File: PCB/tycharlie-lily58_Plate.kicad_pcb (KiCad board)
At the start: 2 copper layers, 146.4 x 104.4 mm, 34 parts

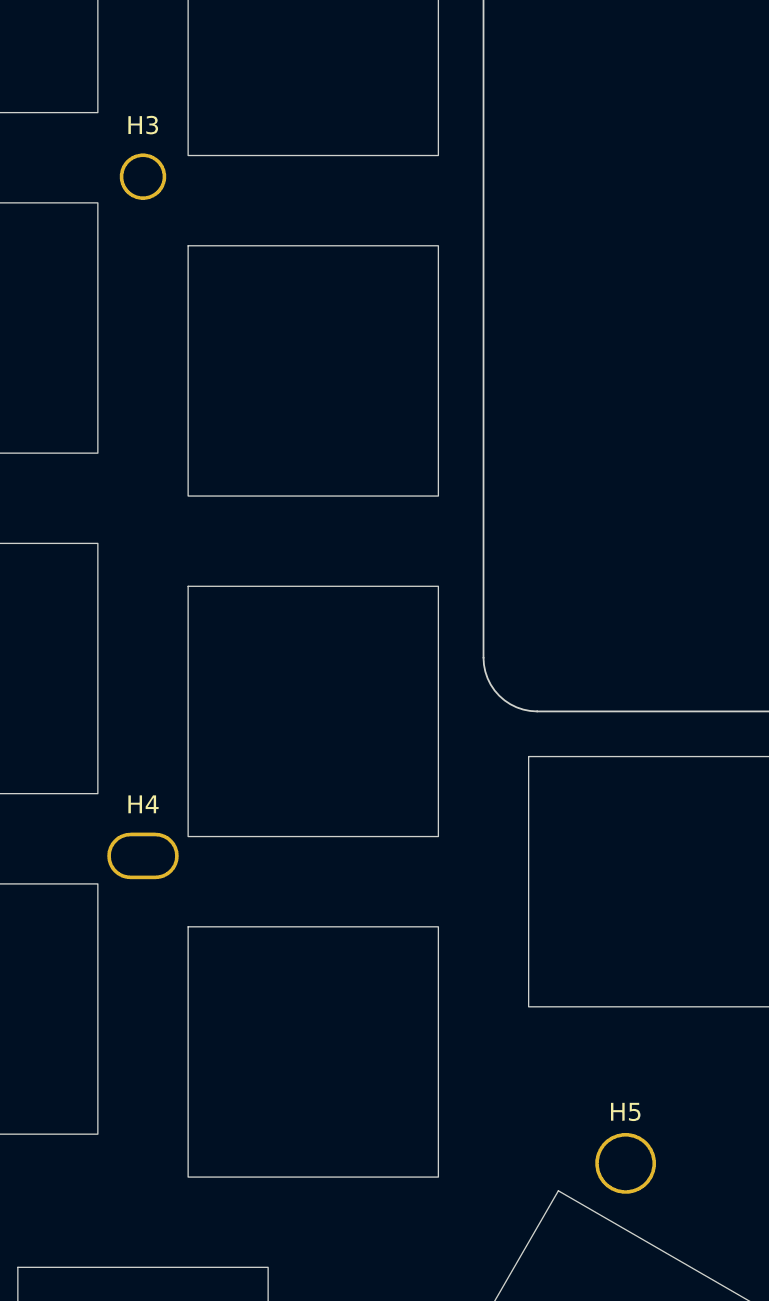
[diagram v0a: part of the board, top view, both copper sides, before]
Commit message: FIX: update the plate mounting hole size
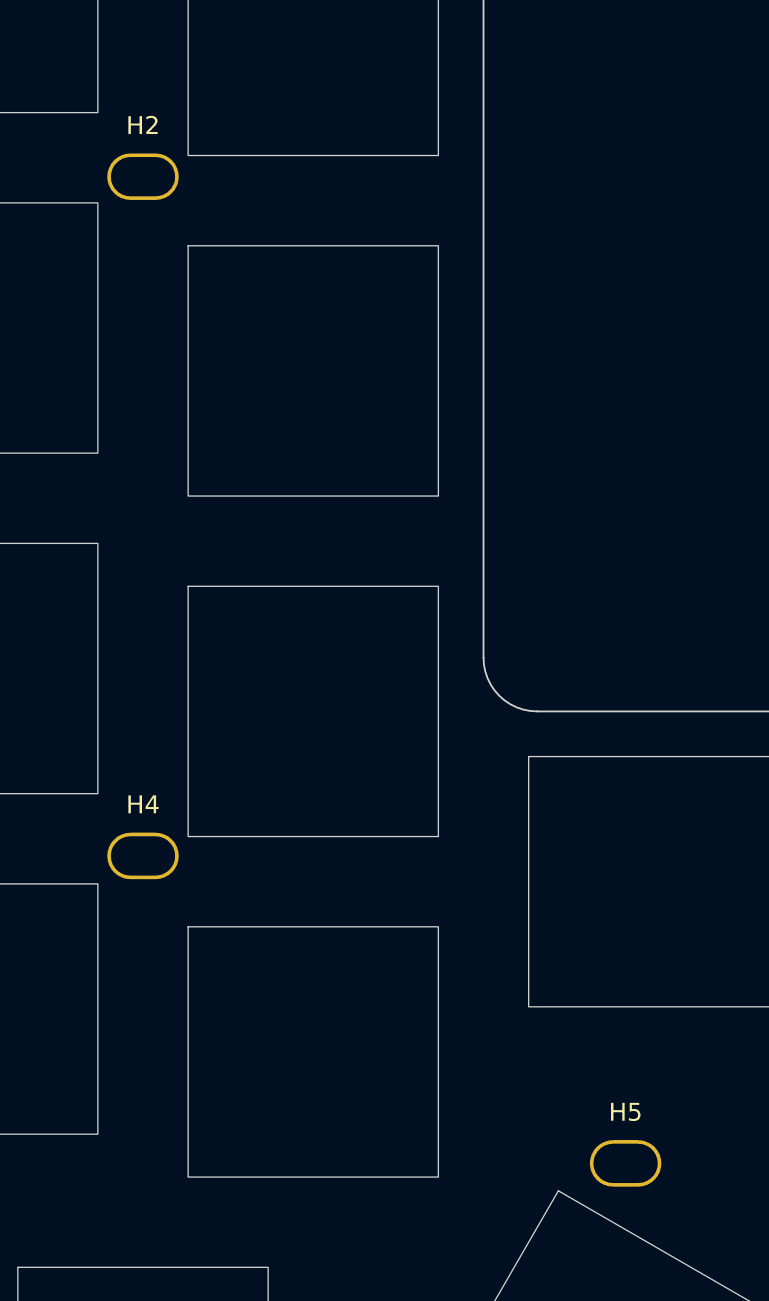
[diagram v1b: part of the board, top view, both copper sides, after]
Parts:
- removed H3: MountingHole_Pad, tycharlie-lily58:MountingHole_2.2mm_M2_ISO14580_Pad_TopBottom
- added H2: MountingHole_3mm_Oval_Hole_ISO14580_Pad_TopBottom, tycharlie-lily58:MountingHole_3mm_Oval_Hole_ISO14580_Pad_TopBottom, F.Cu at (157.2, 50.1)
- H5: value MountingHole_Pad -> MountingHole_3mm_Oval_Hole_ISO14580_Pad_TopBottom; footprint tycharlie-lily58:MountingHole_3mm_M2_ISO14580_Pad_TopBottom -> tycharlie-lily58:MountingHole_3mm_Oval_Hole_ISO14580_Pad_TopBottom

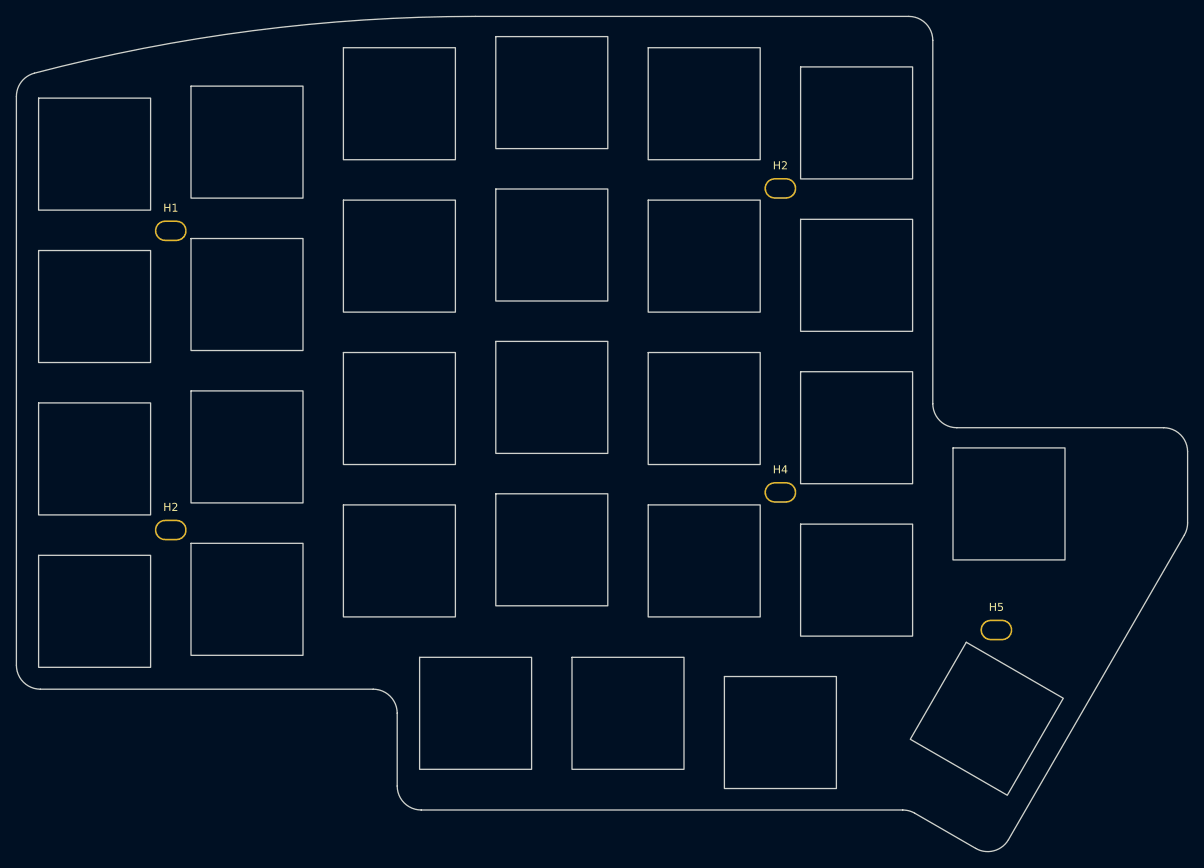
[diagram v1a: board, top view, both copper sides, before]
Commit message: CHORE: add the name on pcb
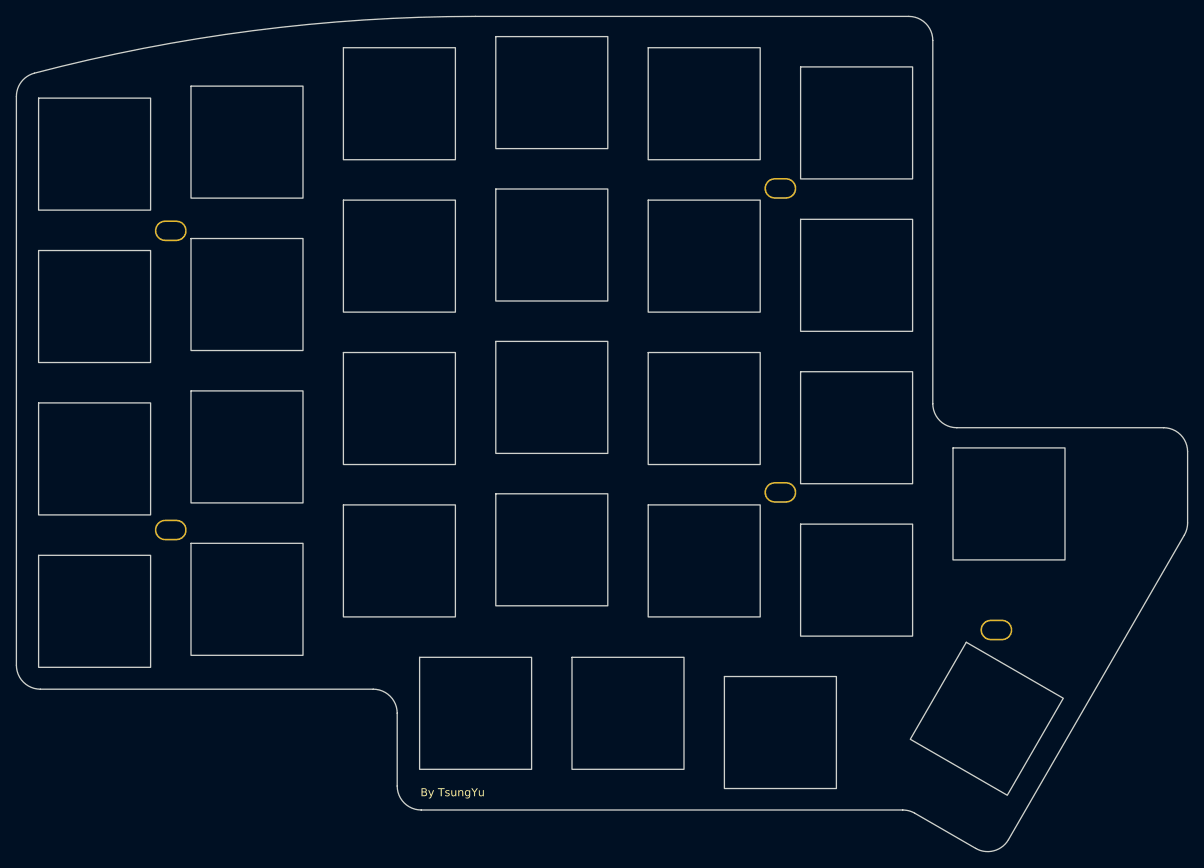
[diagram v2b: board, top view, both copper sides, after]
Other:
- board text added: "By TsungYu"
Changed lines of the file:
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@@
 			(at 0 -2.85 0)
 			(layer "F.SilkS")
+			(hide yes)
 			(effects
 				(font
@@
 			(at 0 -2.85 0)
 			(layer "F.SilkS")
+			(hide yes)
 			(effects
 				(font
@@
 			(at 0 -2.85 0)
 			(layer "F.SilkS")
+			(hide yes)
 			(effects
 				(font
@@
 			(at 0 -2.85 0)
 			(layer "F.SilkS")
+			(hide yes)
 			(effects
 				(font
@@
 			(at 0 -2.85 0)
 			(layer "F.SilkS")
+			(hide yes)
 			(effects
 				(font
@@
 		(layer "Edge.Cuts")
 	)
+	(gr_text "By TsungYu"
+		(at 112.16304 126.17516 0)
+		(layer "F.SilkS")
+		(effects
+			(font
+				(size 1 1)
+				(thickness 0.1)
+			)
+			(justify left bottom)
+		)
+	)
+	(gr_text "By TsungYu"
+		(at 120.86304 126.17516 -0)
+		(layer "B.SilkS")
+		(effects
+			(font
+				(size 1 1)
+				(thickness 0.1)
+			)
+			(justify left bottom mirror)
+		)
+	)
 	(dimension

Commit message: FEAT: update plate mounting hole size
  - change the mounting hole to 5mm
  - renamed the mounting hole footprint name
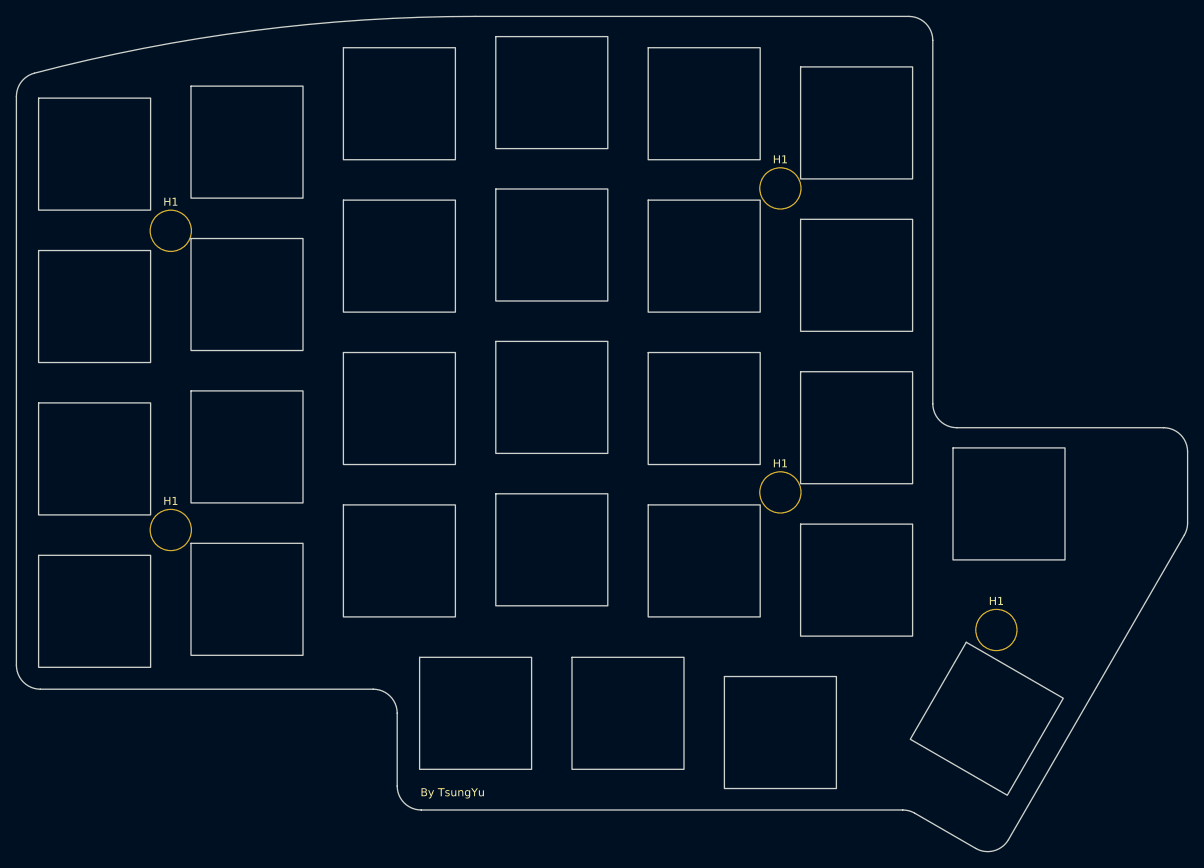
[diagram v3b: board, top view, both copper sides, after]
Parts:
- removed the H1 at (81.0, 55.4)
- removed the H2 at (157.2, 50.1)
- removed H4: MountingHole_Pad, tycharlie-lily58:MountingHole_3mm_Oval_Hole_ISO14580_Pad_TopBottom
- removed H5: MountingHole_3mm_Oval_Hole_ISO14580_Pad_TopBottom, tycharlie-lily58:MountingHole_3mm_Oval_Hole_ISO14580_Pad_TopBottom
- added H1: MountingHole_5mm_Pad_TopBottom, tycharlie-lily58:MountingHole_5mm_Pad_TopBottom, F.Cu at (157.2, 50.1)
- added H1: MountingHole_5mm_Pad_TopBottom, tycharlie-lily58:MountingHole_5mm_Pad_TopBottom, F.Cu at (81.0, 55.4)
- added H1: MountingHole_5mm_Pad_TopBottom, tycharlie-lily58:MountingHole_5mm_Pad_TopBottom, F.Cu at (157.2, 88.1)
- added H1: MountingHole_5mm_Pad_TopBottom, tycharlie-lily58:MountingHole_5mm_Pad_TopBottom, F.Cu at (81.0, 92.8)
- added H1: MountingHole_5mm_Pad_TopBottom, tycharlie-lily58:MountingHole_5mm_Pad_TopBottom, F.Cu at (184.2, 105.3)
